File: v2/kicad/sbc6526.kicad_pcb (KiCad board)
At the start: 4 copper layers, 100 x 100 mm, 61 parts, among them J1 Conn_01x10_Female, P1 2k, P2 5k, SW1 UP, SW2 DOWN, SW3 OK, SW4 CANCEL, SW5 RESET, U1 6526, U10 74AC138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

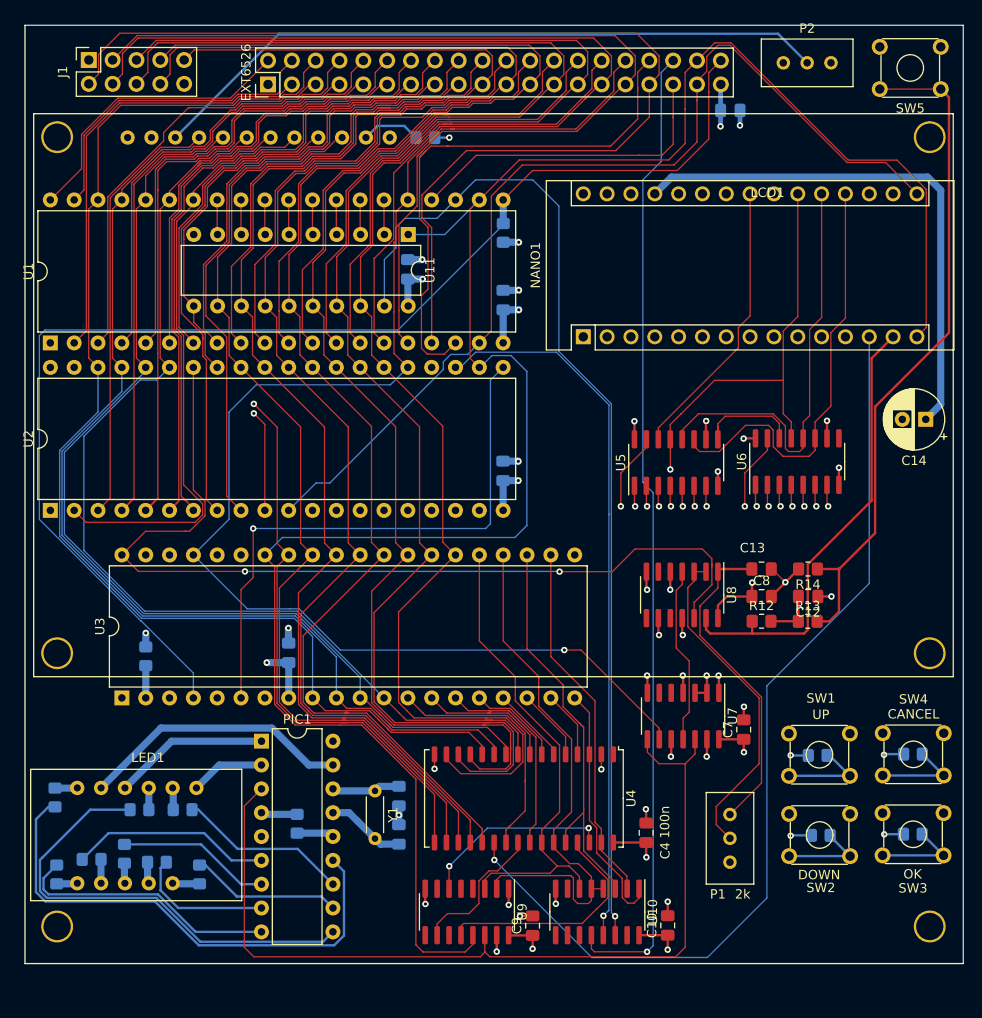
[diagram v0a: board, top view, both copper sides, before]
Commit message: PCB Tweaks
Tracks optimized.
SMD components moved to top layer.
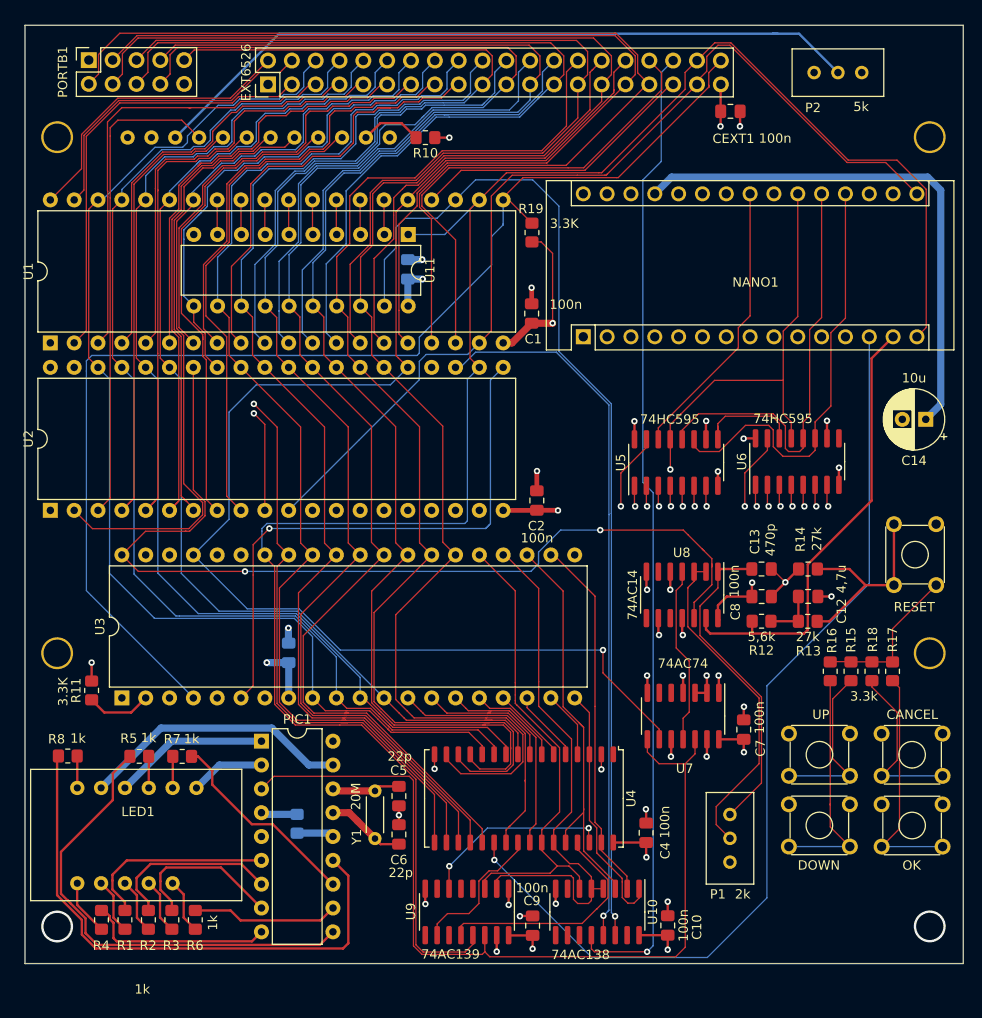
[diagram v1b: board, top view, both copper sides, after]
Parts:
- removed ? (x2): , 
- removed J1: Conn_01x10_Female, Connector_PinSocket_2.54mm:PinSocket_2x05_P2.54mm_Vertical
- added PORTB1: Conn_01x10_Female, Connector_PinSocket_2.54mm:PinSocket_2x05_P2.54mm_Vertical, F.Cu at (106.8, 53.7)
- C1, C2, C5, C6, CEXT1, R1, R10, R11, R15, R16, R17, R18, R19, R2, R3, R4, R5, R6, R7, R8: moved to F.Cu
- moved SW5 53.1 mm to (192.6, 109.7), turned to 90 degrees
- moved R16 17.5 mm to (185.8, 118.8), turned to -90 degrees
- moved R17 17.5 mm to (192.5, 118.8), turned to -90 degrees
- moved R18 9.86 mm to (190.3, 118.8), turned to -90 degrees
- moved R15 9.65 mm to (188.0, 118.8), turned to -90 degrees
- moved R2 7.49 mm to (113.2, 145.3)
- moved R1 7.35 mm to (110.7, 145.3), turned to -90 degrees
- moved R11 6.83 mm to (107.1, 120.9)
- moved R4 6.80 mm to (108.2, 145.3)
- moved R3 6.34 mm to (115.7, 145.3), turned to -90 degrees
- moved R5 5.69 mm to (112.2, 127.9)
- moved R7 5.68 mm to (116.8, 127.9)
- moved R6 4.86 mm to (118.2, 145.3)
- moved C2 4.79 mm to (154.6, 100.7)
- moved R8 4.62 mm to (104.6, 127.9), turned to 0 degrees
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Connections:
- net /bootstrap/A0 renamed A0
- net /bootstrap/A1 renamed A1
- net /bootstrap/A10 renamed A10
- net /bootstrap/A11 renamed A11
- net /bootstrap/A12 renamed A12
- net /bootstrap/A13 renamed A13
- net /bootstrap/A14 renamed A14
- net /bootstrap/A15 renamed A15
- net /bootstrap/A2 renamed A2
- net /bootstrap/A3 renamed A3
- net /bootstrap/A4 renamed A4
- net /bootstrap/A5 renamed A5
- net /bootstrap/A6 renamed A6
- net /bootstrap/A7 renamed A7
- net /bootstrap/A8 renamed A8
- net /bootstrap/A9 renamed A9
- net /bootstrap/BE renamed /BE
- net /bootstrap/D0 renamed D0
- net /bootstrap/D1 renamed D1
- net /bootstrap/D2 renamed D2
- net /bootstrap/D3 renamed D3
- net /bootstrap/D4 renamed D4
- net /bootstrap/D5 renamed D5
- net /bootstrap/D6 renamed D6
- net /bootstrap/D7 renamed D7
- net /bootstrap/RESET renamed /RESET
- net /clock/~PHI2 renamed /~PHI2
- net /io/PB0 renamed /PB0
- net /io/PB1 renamed /PB1
- net /io/PB2 renamed /PB2
- net /io/PB3 renamed /PB3
- net /io/PB4 renamed /PB4
- net /io/PB5 renamed /PB5
- net /io/PB6 renamed /PB6
- net /io/PB7 renamed /PB7
- net /io/VPB4 renamed /VPB4
- net /io/VPB5 renamed /VPB5
- net /io/VPB6 renamed /VPB6
- net /io/VPB7 renamed /VPB7
- net /memory/~CIA renamed /~CIA
- net /memory/~CIAEXT renamed /~CIAEXT
- net /memory/~VIA renamed /~VIA
- net Net-(NANO1-Pad1) renamed no_connect_119
- net Net-(NANO1-Pad17) renamed no_connect_120
- net Net-(NANO1-Pad18) renamed no_connect_121
- net Net-(NANO1-Pad2) renamed no_connect_122
- net Net-(NANO1-Pad22) renamed no_connect_123
- net Net-(NANO1-Pad24) renamed no_connect_124
- net Net-(NANO1-Pad25) renamed no_connect_125
- net Net-(NANO1-Pad28) renamed no_connect_126
- net Net-(NANO1-Pad3) renamed no_connect_127
- net Net-(NANO1-Pad30) renamed no_connect_128
- net Net-(P1-Pad3) renamed no_connect_129
- net Net-(PIC1-Pad18) renamed no_connect_130
- net Net-(R11-Pad1) renamed /cpu/RDY
- net Net-(U10-Pad10) renamed no_connect_131
- net Net-(U10-Pad11) renamed no_connect_132
- net Net-(U10-Pad15) renamed no_connect_133
- net Net-(U10-Pad7) renamed no_connect_134
- net Net-(U10-Pad9) renamed no_connect_135
- net Net-(U2-Pad12) renamed no_connect_136
- net Net-(U2-Pad13) renamed no_connect_137
- net Net-(U2-Pad18) renamed no_connect_138
- net Net-(U2-Pad19) renamed no_connect_139
- net Net-(U2-Pad39) renamed no_connect_140
- net Net-(U2-Pad40) renamed no_connect_141
- net Net-(U3-Pad1) renamed no_connect_142
- net Net-(U3-Pad3) renamed no_connect_143
- net Net-(U3-Pad39) renamed no_connect_144
- net Net-(U3-Pad5) renamed no_connect_145
- net Net-(U3-Pad7) renamed no_connect_146
- net Net-(U4-Pad1) renamed no_connect_147
- net Net-(U6-Pad9) renamed no_connect_148
- net Net-(U7-Pad5) renamed no_connect_149
- net Net-(U7-Pad6) renamed no_connect_150
- net Net-(U8-Pad10) renamed no_connect_151
- net Net-(U8-Pad6) renamed no_connect_152
- net Net-(U8-Pad8) renamed no_connect_153
- net Net-(U9-Pad11) renamed no_connect_154
- net Net-(U9-Pad4) renamed no_connect_155
- net Net-(U9-Pad5) renamed no_connect_156
- net Net-(U9-Pad7) renamed no_connect_157
- net Net-(U9-Pad9) renamed no_connect_158
- LCD1 pad : GND -> (no net)
- U3 pad 35: Net-(U3-Pad35) -> (no net)
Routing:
- net Net-(R13-Pad2): track 72.5 -> 22.1 mm
- net VCC: track 144.3 -> 161.5 mm, vias 26 -> 21
- net /VPB6: track 98.9 -> 114.2 mm
- net /R~W: track 221.4 -> 208.1 mm
- net A3: track 172.8 -> 159.6 mm
- net GND: track 47.8 -> 60.7 mm, vias 25 -> 27
- net /VPB5: track 104.4 -> 116.8 mm
- net A2: track 173.1 -> 163.0 mm
- net /VPB4: track 96.7 -> 105.9 mm
- net /VPB7: track 87.4 -> 95.9 mm
- net Net-(PIC1-Pad9): track 28.3 -> 20.0 mm
- net A0: track 183.0 -> 174.9 mm
- net /peripherals/~EXTPC: track 58.6 -> 51.1 mm
- net A1: track 172.7 -> 165.3 mm
- net /peripherals/LCD_RS: track 46.0 -> 51.9 mm
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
